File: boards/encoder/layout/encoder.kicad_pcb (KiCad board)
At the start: 2 copper layers, 9.6 x 14.1 mm, 3 parts, among them J1 EncoderTab, U1 AS5047U-HTSM

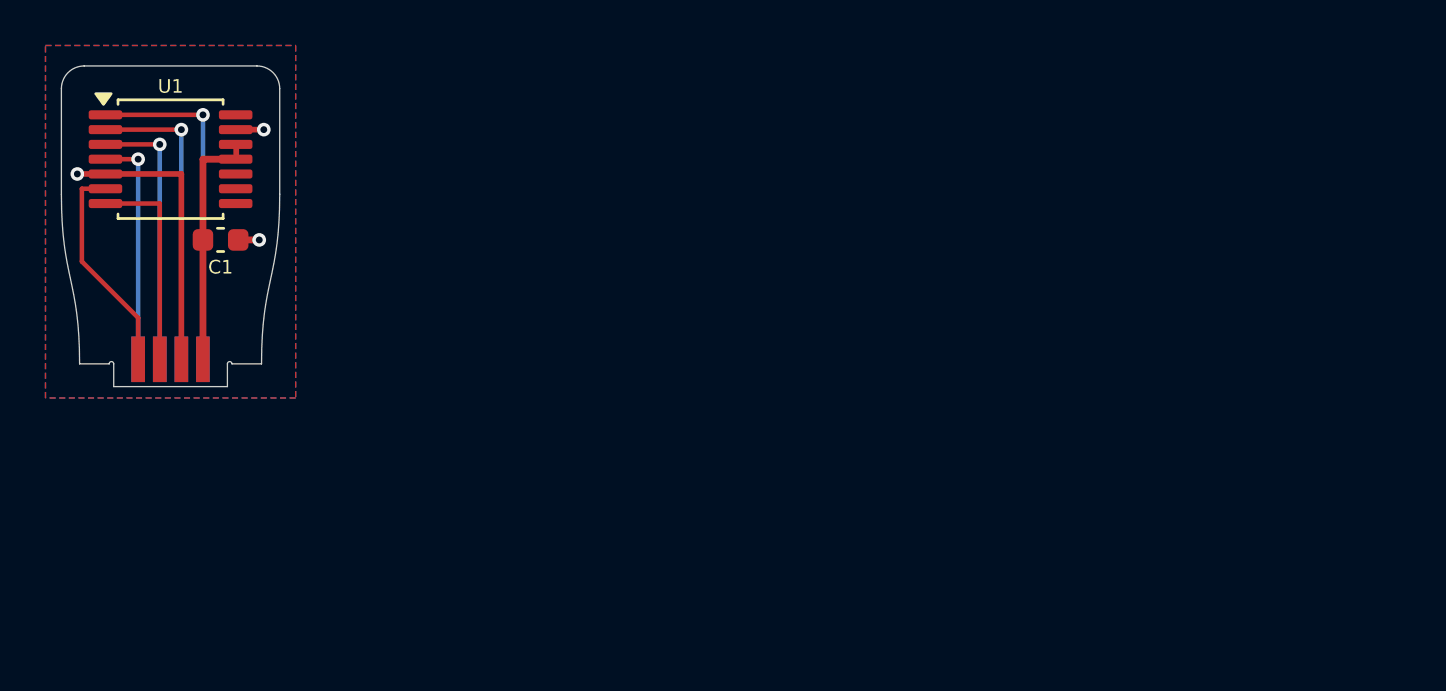
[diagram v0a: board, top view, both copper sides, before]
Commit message: 🚚 Replicate the previous encoder board
The circuit, designators (IC1, C1, J1) and net names of the Altium
MicrasEncoder design, with C1 as the equivalent JLCPCB basic part
(Yageo CC0603KRX7R9BB104 for the Fenghua 0603B104K500NT). The layout
comes from the PcbDoc through boards/encoder/previous/transfer_layout.py:
tracks, vias, pours, teardrops (as plain zones), outline, silkscreen and
logo copied, IC1 and J1 at their previous positions, C1 fitted on the
previous pads.

spec/encoder.toml now checks the outline (layout geometry) instead of
generating it: tab, reliefs, shoulder, tapers (fitted Bezier, 0.021 mm),
corners and extents; thickness 0.79 mm from the PcbDoc stack; the mech
JSON exports the layout outline. `make previous` compares every board
with a previous/board.json.
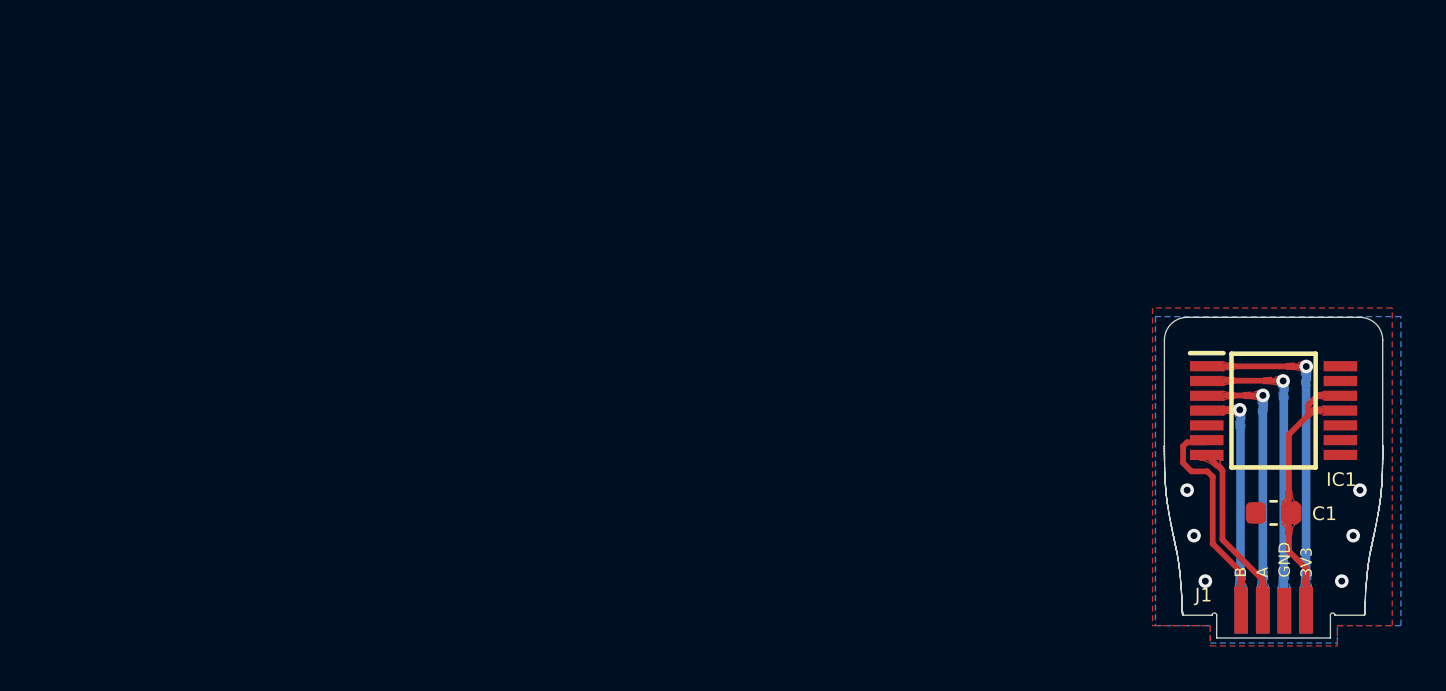
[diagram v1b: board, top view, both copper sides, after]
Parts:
- removed U1: AS5047U-HTSM, Team-Micras_MicrasPCB_components_ams_AS5047U:TSSOP-14_4.4x5mm_P0.65mm
- added IC1: AS5047U-HTSM, Team-Micras_MicrasPCB_components_ams_AS5047U:SOP65P640X120-14N, F.Cu at (148.5, 102.1)
- C1: value 100nF 50V X7R -> 100nF 10% 50V X7R
- J1: footprint Team-Micras_MicrasPCB_components_micras_EncoderTab:EncoderTab_2x4_P0.95mm_Edge -> Team-Micras_MicrasPCB_components_micras_EncoderTab:ENCODER_CONN
- moved J1 49.7 mm to (148.5, 110.9), turned to 90 degrees
- moved C1 47.8 mm to (148.5, 106.6), turned to 180 degrees
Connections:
- J1 pad 1: SPI_CS -> Encoder_CSn
- J1 pad 2: SPI_CLK -> SPI_SCK
- J1 pad 7: ENC_A -> Encoder_ABI_A
- J1 pad 8: ENC_B -> Encoder_ABI_B
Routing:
- net Encoder_CSn: track 0.00 -> 15.2 mm, vias 0 -> 1
- net SPI_CS: track 15.1 -> 0.00 mm, vias 1 -> 0
- net GND: track 14.9 -> 0.00 mm, vias 3 -> 6
- net SPI_SCK: track 0.00 -> 13.5 mm, vias 0 -> 1
- net SPI_CLK: track 13.5 -> 0.00 mm, vias 1 -> 0
- net Encoder_ABI_B: track 0.00 -> 9.87 mm
- net ENC_B: track 9.54 -> 0.00 mm
- net ENC_A: track 9.26 -> 0.00 mm
- net Encoder_ABI_A: track 0.00 -> 7.89 mm
- net 3V3: track 10.9 -> 12.9 mm
- added copper zone on F.Cu, net 3V3
- added copper zone on F.Cu, net Encoder_ABI_A
- added copper zone on F.Cu, net Encoder_ABI_B
- added copper zone on B.Cu, net Encoder_CSn
- added copper zone on F.Cu, net Encoder_CSn
- added copper zone on B.Cu, net SPI_MISO
- added copper zone on F.Cu, net SPI_MISO
- added copper zone on B.Cu, net SPI_MOSI
- added copper zone on F.Cu, net SPI_MOSI
- added copper zone on B.Cu, net SPI_SCK
- added copper zone on F.Cu, net SPI_SCK
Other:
- outline, holes or cut-outs redrawn
- board text added: "3V3"
- board text added: "A"
- board text added: "B"
- board text added: "CSn"
- board text added: "GND"
- board text added: "MISO"
- board text added: "MOSI"
- board text added: "SCK"

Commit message: 🚚 Transfer the Altium pour, teardrop and outline settings to the layouts
The transfer scripts now carry what KiCad's Altium importer drops, and
the layouts are regenerated with them:

- Teardrops (converted to plain zones) fill with a 0.1 mm minimum width
  instead of the importer's 0.25 mm, which left 652 of 786 (main), 5 of
  25 (encoder) and 10 of 46 (bluetooth) teardrops without copper. 0.1 mm
  is JLCPCB's minimum copper feature: 0.0254 mm fills slightly more but
  fails the DFM feature width on all three boards.
- Pours use the Altium polygons' neck width as minimum width (0.1 mm;
  0.4 mm on the encoder's bottom pour, which keeps it out of the channels
  between the SPI tracks, 0.3 mm on the bluetooth plug pour).
- Inner-layer pours relieve through-hole pads (0.254 mm spokes and gap,
  Altium rule PolygonConnect); outer pours stay solid.
- Main In1/In2 keep Altium's 1.559 / 2.074 mm voids around H1-H4
  (copper-pour keepouts).
- Edge.Cuts lines under 1 um (main 6, encoder 1, bluetooth 7) are left
  out and their neighbours joined, so KiCad reads the outlines as valid.
- The board mask expansion is copied from the previous board (0.02 mm);
  main takes the spec's aux origin.
- D4/D5 and bluetooth D1 3D models are scaled to the datasheet heights.
- rework.py catches all six teardrops of the removed C1 VBAT chain (three
  were left as stubs, invisible while unfilled).
- The encoder drops an embedded TSSOP-14 STEP no footprint uses; the
  bluetooth script calls previous.altium_pcb (renamed).

The main layout footprints were resynced from their packages
(pcb layout --sync-footprints), which brings the new WallSensor
silkscreen, R31-R33 and U2's keepouts on all four copper layers.
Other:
- rule pad_to_mask_clearance: 0 -> 0.02
